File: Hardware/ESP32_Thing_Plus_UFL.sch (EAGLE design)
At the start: 49 parts, among them Q1 2.5A/30V, Q2 MBT3904DW1T1, U1 MCP73831, U3 AP2112K-3.3V, U4 CP210X, U5 ESP-WROOM-32EU

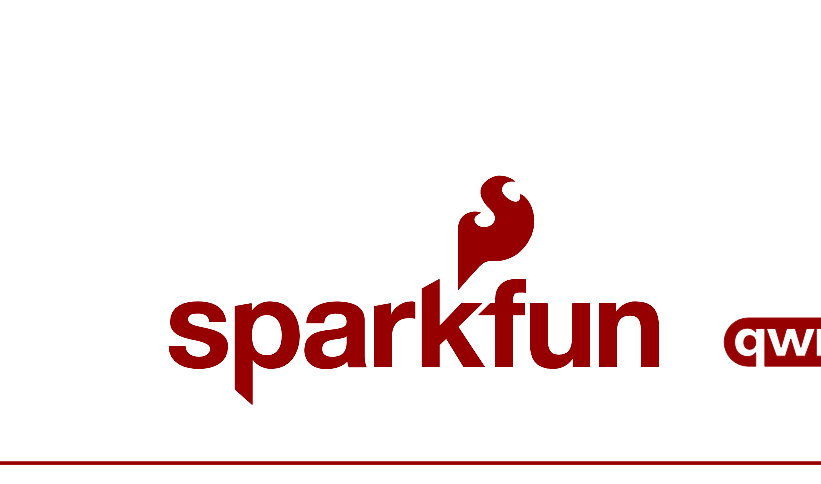
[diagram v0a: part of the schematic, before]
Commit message: Silk Update
Updated silk on bottom
Added "Doot" to GPIO0 button
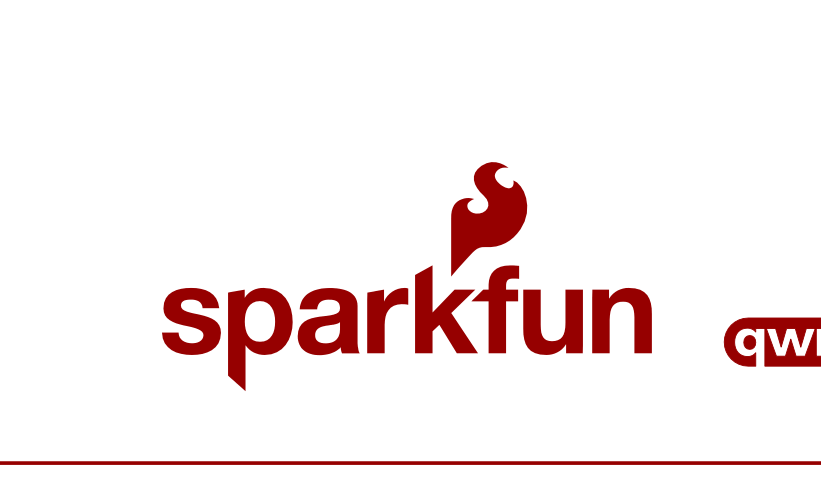
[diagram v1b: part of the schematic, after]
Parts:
- removed LOGO3, LOGO5: SFE_LOGO_NAME_FLAME.1_INCH, SparkFun-Aesthetics:SFE_LOGO_NAME_FLAME.1_INCH
- added LOGO1: SFE_LOGO_NAME_FLAME.1_INCH, SparkFun-Aesthetics:SFE_LOGO_NAME_FLAME.1_INCH
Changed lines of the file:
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@@
 <drawing>
 <settings>
-<setting alwaysvectorfont="no"/>
+<setting alwaysvectorfont="yes"/>
 <setting keepoldvectorfont="yes"/>
 <setting verticaltext="up"/>
@@
 <layer number="128" name="_bValues" color="7" fill="1" visible="yes" active="yes"/>
 <layer number="129" name="Mask" color="7" fill="1" visible="yes" active="yes"/>
+<layer number="130" name="SMDSTROOK" color="7" fill="1" visible="no" active="no"/>
 <layer number="131" name="tAdjust" color="7" fill="1" visible="yes" active="yes"/>
 <layer number="132" name="bAdjust" color="7" fill="1" visible="yes" active="yes"/>
+<layer number="133" name="bottom_silk" color="7" fill="1" visible="no" active="no"/>
+<layer number="134" name="silk_top" color="7" fill="1" visible="no" active="no"/>
+<layer number="135" name="silk_bottom" color="7" fill="1" visible="no" active="no"/>
+<layer number="136" name="silktop" color="7" fill="1" visible="no" active="no"/>
+<layer number="137" name="silkbottom" color="7" fill="1" visible="no" active="no"/>
+<layer number="138" name="EEE" color="7" fill="1" visible="no" active="no"/>
+<layer number="139" name="_tKeepout" color="7" fill="1" visible="no" active="no"/>
+<layer number="140" name="mbKeepout" color="7" fill="1" visible="no" active="no"/>
+<layer number="141" name="ASSEMBLY_TOP" color="7" fill="1" visible="no" active="no"/>
+<layer number="142" name="mbRestrict" color="7" fill="1" visible="no" active="no"/>
+<layer number="143" name="PLACE_BOUND_TOP" color="7" fill="1" visible="no" active="no"/>
 <layer number="144" name="Drill_legend" color="7" fill="1" visible="yes" active="yes"/>
+<layer number="145" name="DrillLegend_01-16" color="7" fill="1" visible="no" active="no"/>
+<layer number="146" name="DrillLegend_01-20" color="7" fill="1" visible="no" active="no"/>
+<layer number="147" name="PIN_NUMBER" color="7" fill="1" visible="no" active="no"/>
+<layer number="149" name="DrillLegend_02-15" color="7" fill="1" visible="no" active="no"/>
 <layer number="150" name="Notes" color="7" fill="1" visible="yes" active="yes"/>
 <layer number="151" name="HeatSink" color="7" fill="1" visible="yes" active="yes"/>
@@
 <layer number="154" name="FabDoc2" color="7" fill="1" visible="yes" active="yes"/>
 <layer number="155" name="FabDoc3" color="7" fill="1" visible="yes" active="yes"/>
+<layer number="166" name="AntennaArea" color="7" fill="1" visible="no" active="no"/>
+<layer number="168" name="4mmHeightArea" color="7" fill="1" visible="no" active="no"/>
+<layer number="191" name="mNets" color="7" fill="1" visible="no" active="no"/>
+<layer number="192" name="mBusses" color="7" fill="1" visible="no" active="no"/>
+<layer number="193" name="mPins" color="7" fill="1" visible="no" active="no"/>
+<layer number="194" name="mSymbols" color="7" fill="1" visible="no" active="no"/>
+<layer number="195" name="mNames" color="7" fill="1" visible="no" active="no"/>
+<layer number="196" name="mValues" color="7" fill="1" visible="no" active="no"/>
 <layer number="199" name="Contour" color="7" fill="1" visible="yes" active="yes"/>
 <layer number="200" name="200bmp" color="1" fill="10" visible="yes" active="yes"/>
@@
 <part name="GND5" library="SparkFun-Aesthetics" deviceset="GND" device=""/>
 <part name="R8" library="SparkFun-Resistors" deviceset="100KOHM" device="-0402T-1/16W-1%" value="100k"/>
-<part name="LOGO3" library="SparkFun-Aesthetics" deviceset="SFE_LOGO_NAME_FLAME" device=".1_INCH"/>
 <part name="LOGO4" library="SparkFun-Aesthetics" deviceset="FOUR_LAYER_WARNING" device=""/>
 <part name="FD1" library="SparkFun-Aesthetics" deviceset="FIDUCIAL" device="UFIDUCIAL"/>
@@
 <part name="R9" library="SparkFun-Resistors" deviceset="33KOHM" device="-0402T-1/16W-1%" value="33k"/>
 <part name="GND3" library="SparkFun-Aesthetics" deviceset="GND" device=""/>
-<part name="LOGO5" library="SparkFun-Aesthetics" deviceset="SFE_LOGO_NAME_FLAME" device=".1_INCH"/>
 <part name="C2" library="SparkFun-Capacitors" deviceset="0.1UF" device="-0402T-16V-10%" value="0.1uF"/>
 <part name="C3" library="SparkFun-Capacitors" deviceset="4.7UF" device="-0402_TIGHT-6.3V-20%-X5R" value="4.7uF"/>
@@
 <part name="SUPPLY10" library="SparkFun-PowerSymbols" deviceset="3.3V" device=""/>
 <part name="LOGO6" library="SparkFun-Aesthetics" deviceset="QWIIC_LOGO" device="_5MM" value="QWIIC_LOGO_5MM"/>
+<part name="LOGO1" library="SparkFun-Aesthetics" deviceset="SFE_LOGO_NAME_FLAME" device=".1_INCH"/>
 </parts>
 <sheets>
@@
 <attribute name="VALUE" x="63.5" y="234.696" size="1.778" layer="96" font="vector" align="top-center"/>
 </instance>
-<instance part="LOGO3" gate="G$1" x="51.562" y="6.096" smashed="yes"/>
 <instance part="LOGO4" gate="G$1" x="393.7" y="38.1" smashed="yes"/>
 <instance part="FD1" gate="G$1" x="429.26" y="33.02" smashed="yes"/>
@@
 <attribute name="VALUE" x="314.96" y="210.82" size="1.778" layer="96" font="vector"/>
 </instance>
-<instance part="LOGO5" gate="G$1" x="51.562" y="6.096" smashed="yes"/>
 <instance part="C2" gate="G$1" x="401.32" y="210.82" smashed="yes">
 <attribute name="NAME" x="402.844" y="213.741" size="1.778" layer="95" font="vector"/>
@@
 </instance>
 <instance part="LOGO6" gate="G$1" x="122.174" y="13.462" smashed="yes"/>
+<instance part="LOGO1" gate="G$1" x="50.8" y="7.62" smashed="yes"/>
 </instances>
 <busses>
